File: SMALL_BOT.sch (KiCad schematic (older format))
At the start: 22 parts, among them J1 MOTOR_B, J10 HEADER_2, J11 Conn_01x04, J2 MOTOR_A, J3 HEADER_2, J4 HEADER_2, J5 Conn_01x04, J6 Conn_01x04, J7 Conn_01x04, J8 Conn_01x04, J9 HEADER_2, Q1 2N7002, U1 Teensy4.0, U2 DRV8833_POLOLU, U3 LM1117-SOT

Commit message: se modifico pcb
se movieron de lugar los conectores para los sensores ultrasonidos y se agrego pantalla oled
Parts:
- removed J3, J4: HEADER_2, EESTN5:Pin_strip_2, symbol EESTN5:HEADER_2
- removed U2: DRV8833_POLOLU, EESTN5:DRV8833_Pololu, symbol EESTN5:DRV8833_POLOLU
- added Brd1: SSD1306, SSD1306:128x64OLED, symbol SSD1306-128x64_OLED:SSD1306
- added C4, C6: 100nf, EESTN5:C_1206, symbol EESTN5:C
- added C5, C7: 100uf, EESTN5:CAP_TAN_A, symbol EESTN5:CAPAPOL
- added J12, J14: LEDS, EESTN5:Pin_Strip_3, symbol EESTN5:Conn_01X03
- added J13: I2C, EESTN5:pin_strip_4, symbol EESTN5:Conn_01x04
- added J15, J16, J3, J4: HEADER_1, EESTN5:Cable_Doble_1,5mm, symbol EESTN5:HEADER_1
- added R2, R3: 0,25, EESTN5:R_1206, symbol EESTN5:R
- added R? (x2): 10k, symbol EESTN5:R
- added U2, U4: DRV8872, EESTN5:SSOP-8, symbol EESTN5:DRV8872
- C1: value CAPAPOL -> 1000uf
- C2: value C -> 100nf
- C3: value CAPAPOL -> 10uf
- J5, J6, J7, J8: value Conn_01x04 -> ULTRASONICO; footprint EESTN5:HEADER-4H -> EESTN5:pin_strip_4
- R1: value R -> 10k
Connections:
- net labels added: NEOPIXEL, NEOPIXEL1, SCL, SDA
- wire segments 106 -> 161
- no-connect marks 0 -> 2
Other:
- moved on the sheet: BZ1, D1, Q1, R1

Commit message: Varios
Falta verificar al 100% la compatibilidad con los 3.3v para la Teensy.
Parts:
- removed U1: Teensy4.0, EESTN5:Teensy40, symbol EESTN5:Teensy4.0
- added U1: Teensy4.0_B, EESTN5:Teensy40_B, symbol EESTN5:Teensy4.0_B
- Brd1: symbol SSD1306-128x64_OLED:SSD1306 -> SMALL_BOT-rescue:SSD1306-SSD1306-128x64_OLED
- C6: value 100nf -> 100nF
- C7: value 100uf -> 100uF
- J1, J2: footprint EESTN5:Pololu_Micro_Gear_Motor_W_Mount -> EESTN5:Pololu_Micro_Con_Soporte_Simple
- J10: value HEADER_2 -> JMP
- J11: value Conn_01x04 -> UART
- J5, J6, J7, J8: value ULTRASONICO -> HC-SR04
- J9: value HEADER_2 -> Bateria
- R4, R5: renamed from R?; footprint (none) -> EESTN5:R_1206
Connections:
- wire segments 161 -> 157
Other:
- moved on the sheet: H1, J1, J2
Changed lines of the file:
@@
 $EndDescr
 $Comp
-L EESTN5:Teensy4.0 U1
-U 1 1 5FC8AD44
-P 2000 2300
-F 0 "U1" H 2000 3915 50  0000 C CNN
-F 1 "Teensy4.0" H 2000 3824 50  0000 C CNN
-F 2 "EESTN5:Teensy40" H 1600 2500 50  0001 C CNN
-F 3 "" H 1600 2500 50  0001 C CNN
-	1    2000 2300
-	1    0    0    -1
-$EndComp
-$Comp
 L EESTN5:HEADER_2 J1
 U 1 1 5FC8B78D
-P 10600 650
-F 0 "J1" H 10728 703 60  0000 L CNN
-F 1 "MOTOR_B" H 10728 597 60  0000 L CNN
-F 2 "EESTN5:Pololu_Micro_Gear_Motor_W_Mount" H 10600 900 60  0001 C CNN
-F 3 "" H 10600 900 60  0000 C CNN
-	1    10600 650
+P 10275 725
+F 0 "J1" H 10403 778 60  0000 L CNN
+F 1 "MOTOR_B" H 10403 672 60  0000 L CNN
+F 2 "EESTN5:Pololu_Micro_Con_Soporte_Simple" H 10275 975 60  0001 C CNN
+F 3 "" H 10275 975 60  0000 C CNN
+	1    10275 725
 	1    0    0    -1
 $EndComp
@@
 L EESTN5:HEADER_2 J2
 U 1 1 5FC8BAE6
-P 10600 850
-F 0 "J2" H 10728 903 60  0000 L CNN
-F 1 "MOTOR_A" H 10728 797 60  0000 L CNN
-F 2 "EESTN5:Pololu_Micro_Gear_Motor_W_Mount" H 10600 1100 60  0001 C CNN
-F 3 "" H 10600 1100 60  0000 C CNN
-	1    10600 850
+P 10275 925
+F 0 "J2" H 10403 978 60  0000 L CNN
+F 1 "MOTOR_A" H 10403 872 60  0000 L CNN
+F 2 "EESTN5:Pololu_Micro_Con_Soporte_Simple" H 10275 1175 60  0001 C CNN
+F 3 "" H 10275 1175 60  0000 C CNN
+	1    10275 925
 	1    0    0    -1
 $EndComp
@@
 L EESTN5:Mounting_Hole H1
 U 1 1 5FC8C238
-P 11100 700
-F 0 "H1" H 11200 700 50  0000 L CNN
-F 1 "Mounting_Hole" H 11100 825 50  0001 C CNN
-F 2 "EESTN5:Bateria_Lipo_2S_800mah" H 11100 700 60  0001 C CNN
-F 3 "" H 11100 700 60  0001 C CNN
-	1    11100 700
+P 10975 825
+F 0 "H1" H 11075 825 50  0000 L CNN
+F 1 "Mounting_Hole" H 10975 950 50  0001 C CNN
+F 2 "EESTN5:Bateria_Lipo_2S_800mah" H 10975 825 60  0001 C CNN
+F 3 "" H 10975 825 60  0001 C CNN
+	1    10975 825
 	1    0    0    -1
 $EndComp
@@
 P 1450 5150
 F 0 "J5" H 1530 5142 50  0000 L CNN
-F 1 "ULTRASONICO" H 1530 5051 50  0000 L CNN
+F 1 "HC-SR04" H 1530 5051 50  0000 L CNN
 F 2 "EESTN5:pin_strip_4" H 1450 5150 50  0001 C CNN
 F 3 "~" H 1450 5150 50  0001 C CNN
@@
 P 2750 5150
 F 0 "J7" H 2830 5142 50  0000 L CNN
-F 1 "ULTRASONICO" H 2830 5051 50  0000 L CNN
+F 1 "HC-SR04" H 2830 5051 50  0000 L CNN
 F 2 "EESTN5:pin_strip_4" H 2750 5150 50  0001 C CNN
 F 3 "~" H 2750 5150 50  0001 C CNN
@@
 P 1450 6400
 F 0 "J6" H 1530 6392 50  0000 L CNN
-F 1 "ULTRASONICO" H 1530 6301 50  0000 L CNN
+F 1 "HC-SR04" H 1530 6301 50  0000 L CNN
 F 2 "EESTN5:pin_strip_4" H 1450 6400 50  0001 C CNN
 F 3 "~" H 1450 6400 50  0001 C CNN
@@
 P 2750 6400
 F 0 "J8" H 2830 6392 50  0000 L CNN
-F 1 "ULTRASONICO" H 2830 6301 50  0000 L CNN
+F 1 "HC-SR04" H 2830 6301 50  0000 L CNN
 F 2 "EESTN5:pin_strip_4" H 2750 6400 50  0001 C CNN
 F 3 "~" H 2750 6400 50  0001 C CNN
@@
 U 1 1 5FD09509
 P 7500 5600
-F 0 "J9" H 7492 5313 60  0000 C CNN
-F 1 "HEADER_2" H 7500 5250 60  0000 C CNN
+F 0 "J9" H 7675 5575 60  0000 C CNN
+F 1 "Bateria" H 7575 5800 60  0000 C CNN
 F 2 "Connector_JST:JST_EH_B2B-EH-A_1x02_P2.50mm_Vertical" H 7500 5850 60  0001 C CNN
 F 3 "" H 7500 5850 60  0000 C CNN
@@
 F 1 "LM1117-SOT" H 9200 5701 60  0000 C CNN
 F 2 "EESTN5:SOT223" H 9200 5450 60  0001 C CNN
-F 3 "http://www.mouser.com/ds/2/282/lm1117-n-7107.pdf" H 9200 5595 60  0000 C CNN
+F 3 "http://www.mouser.com/ds/2/282/lm1117-n-7107.pdf" H 9200 5595 60  0001 C CNN
 	1    9200 5450
 	1    0    0    -1
@@
 U 1 1 5FD52493
 P 8150 5550
-F 0 "J10" V 8089 5678 60  0000 L CNN
-F 1 "HEADER_2" V 8195 5678 60  0000 L CNN
+F 0 "J10" V 8300 5475 60  0000 L CNN
+F 1 "JMP" V 8425 5475 60  0000 L CNN
 F 2 "EESTN5:Pin_strip_2" H 8150 5800 60  0001 C CNN
 F 3 "" H 8150 5800 60  0000 C CNN
@@
 P 4700 3350
 F 0 "J11" H 4780 3342 50  0000 L CNN
-F 1 "Conn_01x04" H 4780 3251 50  0000 L CNN
+F 1 "UART" H 4780 3251 50  0000 L CNN
 F 2 "EESTN5:pin_strip_4" H 4700 3350 50  0001 C CNN
 F 3 "~" H 4700 3350 50  0001 C CNN
@@
 Wire Wire Line
 	900  1150 650  1150
-Wire Wire Line
-	900  2550 750  2550
-Wire Wire Line
-	750  2550 750  3750
 $Comp
 L power:GND #PWR0123
 U 1 1 5FD87C3A
-P 750 3900
-F 0 "#PWR0123" H 750 3650 50  0001 C CNN
-F 1 "GND" H 755 3727 50  0000 C CNN
-F 2 "" H 750 3900 50  0001 C CNN
-F 3 "" H 750 3900 50  0001 C CNN
-	1    750  3900
+P 800 3900
+F 0 "#PWR0123" H 800 3650 50  0001 C CNN
+F 1 "GND" H 805 3727 50  0000 C CNN
+F 2 "" H 800 3900 50  0001 C CNN
+F 3 "" H 800 3900 50  0001 C CNN
+	1    800  3900
 	1    0    0    -1
 $EndComp
 Wire Wire Line
 	900  950  800  950
-Wire Wire Line
-	800  950  800  3750
-Wire Wire Line
-	800  3750 750  3750
-Connection ~ 750  3750
-Wire Wire Line
-	750  3750 750  3900
 $Comp
 L EESTN5:Conn_01X03 J12
@@
 NEOPIXEL
 $Comp
-L SSD1306-128x64_OLED:SSD1306 Brd1
+L SMALL_BOT-rescue:SSD1306-SSD1306-128x64_OLED Brd1
 U 1 1 5FE619BA
 P 10300 3600
-F 0 "Brd1" H 10022 3612 50  0000 R CNN
-F 1 "SSD1306" H 10022 3703 50  0000 R CNN
+F 0 "Brd1" H 10475 3200 50  0000 R CNN
+F 1 "SSD1306" H 10475 3300 50  0000 R CNN
 F 2 "SSD1306:128x64OLED" H 10300 3850 50  0001 C CNN
 F 3 "" H 10300 3850 50  0001 C CNN
@@
 P 5750 4550
 F 0 "J3" H 5878 4603 60  0000 L CNN
-F 1 "HEADER_1" H 5878 4497 60  0000 L CNN
+F 1 "HEADER_1" H 5878 4497 60  0001 L CNN
 F 2 "EESTN5:Cable_Doble_1,5mm" H 5750 4800 60  0001 C CNN
 F 3 "" H 5750 4800 60  0000 C CNN
@@
 P 5750 4750
 F 0 "J4" H 5878 4803 60  0000 L CNN
-F 1 "HEADER_1" H 6000 4850 60  0000 L CNN
+F 1 "HEADER_1" H 6000 4850 60  0001 L CNN
 F 2 "EESTN5:Cable_Doble_1,5mm" H 5750 5000 60  0001 C CNN
 F 3 "" H 5750 5000 60  0000 C CNN
@@
 P 5800 6350
 F 0 "J15" H 5928 6403 60  0000 L CNN
-F 1 "HEADER_1" H 5928 6297 60  0000 L CNN
+F 1 "HEADER_1" H 5928 6297 60  0001 L CNN
 F 2 "EESTN5:Cable_Doble_1,5mm" H 5800 6600 60  0001 C CNN
 F 3 "" H 5800 6600 60  0000 C CNN
@@
 P 5800 6550
 F 0 "J16" H 5928 6603 60  0000 L CNN
-F 1 "HEADER_1" H 6050 6650 60  0000 L CNN
+F 1 "HEADER_1" H 6050 6650 60  0001 L CNN
 F 2 "EESTN5:Cable_Doble_1,5mm" H 5800 6800 60  0001 C CNN
 F 3 "" H 5800 6800 60  0000 C CNN
@@
 U 1 1 5FF25413
 P 5600 6900
-F 0 "C6" H 5715 6938 40  0000 L CNN
-F 1 "100nf" H 5715 6862 40  0000 L CNN
+F 0 "C6" H 5325 6925 40  0000 L CNN
+F 1 "100nF" H 5325 6850 40  0000 L CNN
 F 2 "EESTN5:C_1206" H 5638 6750 30  0001 C CNN
 F 3 "" H 5600 6900 60  0000 C CNN
@@
 P 5900 6900
 F 0 "C7" H 6009 6938 40  0000 L CNN
-F 1 "100uf" H 6009 6862 40  0000 L CNN
+F 1 "100uF" H 6009 6862 40  0000 L CNN
 F 2 "EESTN5:CAP_TAN_A" H 6000 6750 30  0001 C CNN
 F 3 "" H 5900 6900 300 0000 C CNN
@@
 	9300 1450 9050 1450
 $Comp
-L EESTN5:R R?
+L EESTN5:R R4
 U 1 1 5FFAA029
 P 9300 3450
-F 0 "R?" H 9150 3500 50  0000 L CNN
+F 0 "R4" H 9150 3500 50  0000 L CNN
 F 1 "10k" H 9150 3400 50  0000 L CNN
-F 2 "" H 9300 3450 60  0000 C CNN
+F 2 "EESTN5:R_1206" H 9300 3450 60  0001 C CNN
 F 3 "" H 9300 3450 60  0000 C CNN
 	1    9300 3450
@@
 Connection ~ 9400 3700
 $Comp
-L EESTN5:R R?
+L EESTN5:R R5
 U 1 1 5FFAA29B
 P 9400 3450
-F 0 "R?" H 9448 3496 50  0000 L CNN
+F 0 "R5" H 9448 3496 50  0000 L CNN
 F 1 "10k" H 9448 3405 50  0000 L CNN
-F 2 "" H 9400 3450 60  0000 C CNN
+F 2 "EESTN5:R_1206" H 9400 3450 60  0001 C CNN
 F 3 "" H 9400 3450 60  0000 C CNN
 	1    9400 3450
@@
 	9400 3300 9400 3350
 Connection ~ 9300 3300
+$Comp
+L EESTN5:Teensy4.0_B U1
+U 1 1 5FD77C20
+P 2000 2300
+F 0 "U1" H 2000 3915 50  0000 C CNN
+F 1 "Teensy4.0_B" H 2000 3824 50  0000 C CNN
+F 2 "EESTN5:Teensy40_B" H 1600 2500 50  0001 C CNN
+F 3 "" H 1600 2500 50  0001 C CNN
+	1    2000 2300
+	1    0    0    -1
+$EndComp
+Wire Wire Line
+	800  950  800  3900
 $EndSCHEMATC

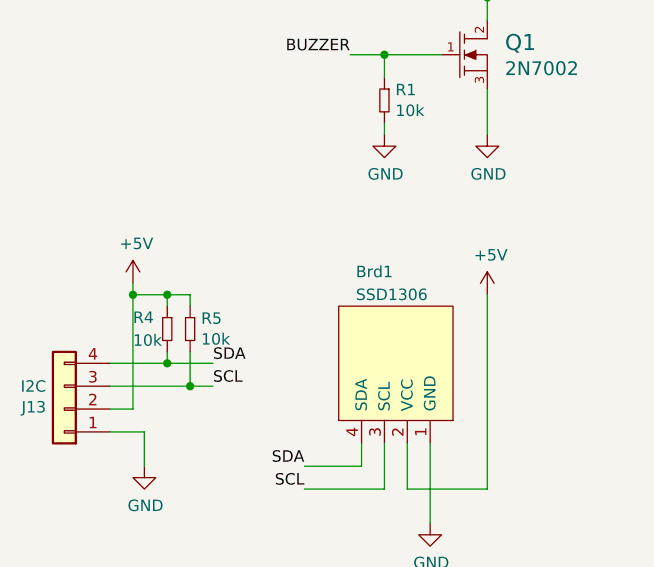
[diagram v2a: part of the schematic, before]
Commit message: Pantalla Oled
Actualice la pantalla oled
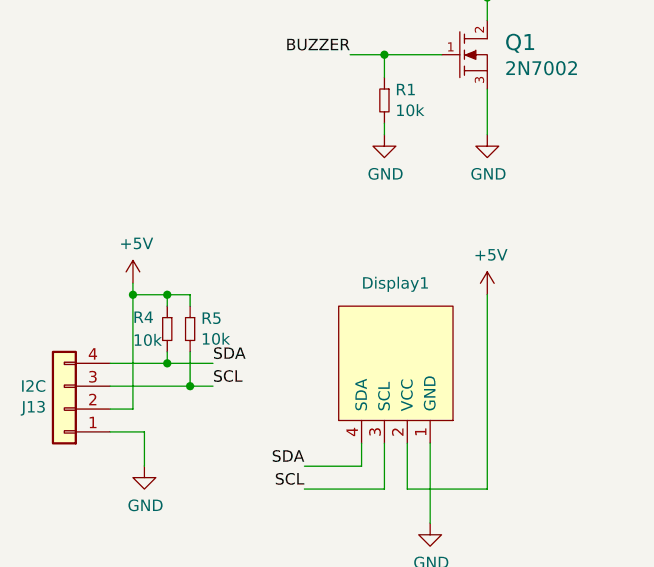
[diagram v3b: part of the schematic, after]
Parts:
- removed Brd1: SSD1306, SSD1306:128x64OLED, symbol SMALL_BOT-rescue:SSD1306-SSD1306-128x64_OLED
- added Display1: SSD1306-SSD1306-128x64_OLED, EESTN5:128x64OLED, symbol EESTN5:SSD1306-SSD1306-128x64_OLED
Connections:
- net +5V: now also Display1.2 (VCC)
- net GND: now also Display1.1 (GND)
- net SCL: now also Display1.3 (SCL)
- net SDA: now also Display1.4 (SDA)
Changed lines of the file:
@@
 Text Label 700  1450 2    50   ~ 0
 NEOPIXEL
-$Comp
-L SMALL_BOT-rescue:SSD1306-SSD1306-128x64_OLED Brd1
-U 1 1 5FE619BA
-P 10300 3600
-F 0 "Brd1" H 10475 3200 50  0000 R CNN
-F 1 "SSD1306" H 10475 3300 50  0000 R CNN
-F 2 "SSD1306:128x64OLED" H 10300 3850 50  0001 C CNN
-F 3 "" H 10300 3850 50  0001 C CNN
-	1    10300 3600
-	-1   0    0    1
-$EndComp
 Wire Wire Line
 	10150 3950 10150 4050
@@
 Wire Wire Line
 	800  950  800  3900
+$Comp
+L EESTN5:SSD1306-SSD1306-128x64_OLED Display1
+U 1 1 5FD81AE7
+P 10300 3600
+F 0 "Display1" H 10450 3250 50  0000 R CNN
+F 1 "SSD1306-SSD1306-128x64_OLED" H 10300 3550 50  0001 C CNN
+F 2 "EESTN5:128x64OLED" H 10300 3850 50  0001 C CNN
+F 3 "" H 10300 3850 50  0001 C CNN
+	1    10300 3600
+	-1   0    0    1
+$EndComp
 $EndSCHEMATC

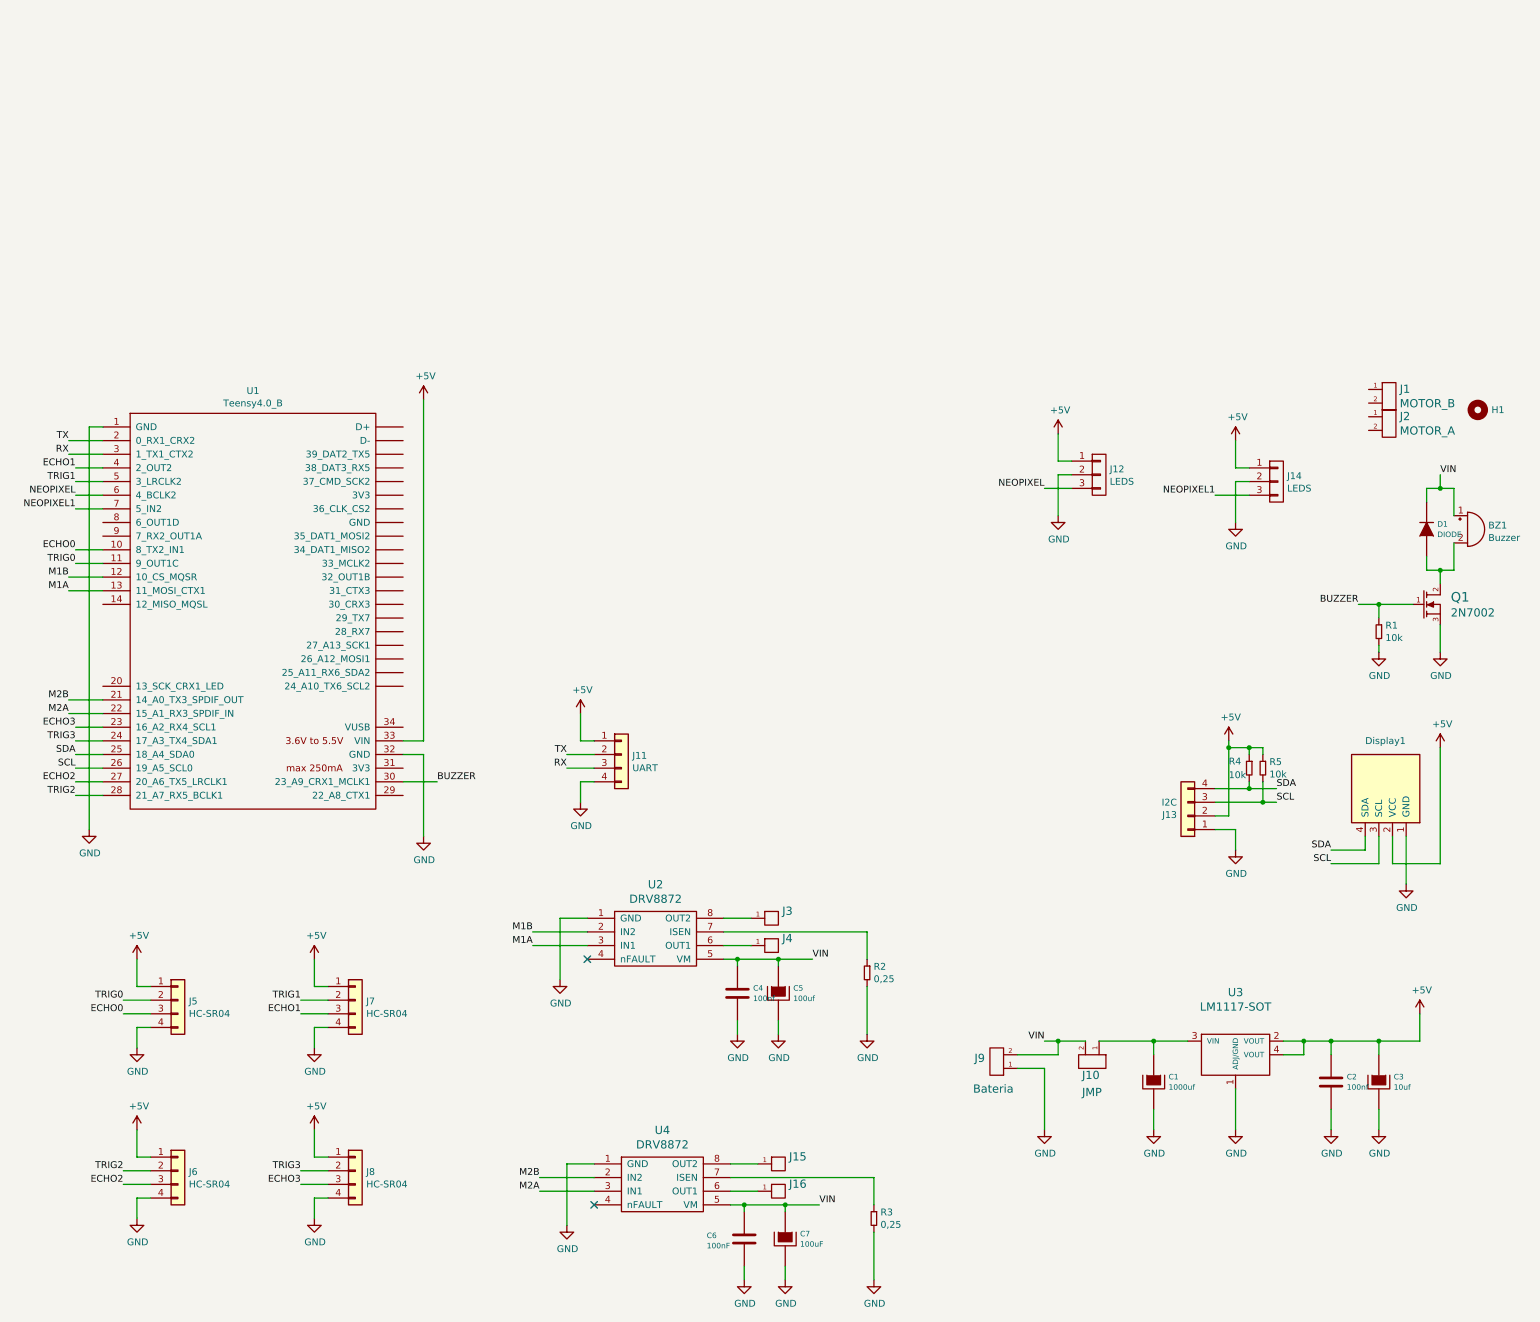
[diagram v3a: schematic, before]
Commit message: modificaciones
se agrego una brebe pinout, se agrego una carpeta "doc" y lista de materiales, hay que agregarle los precios.tambien se modifico el pcb
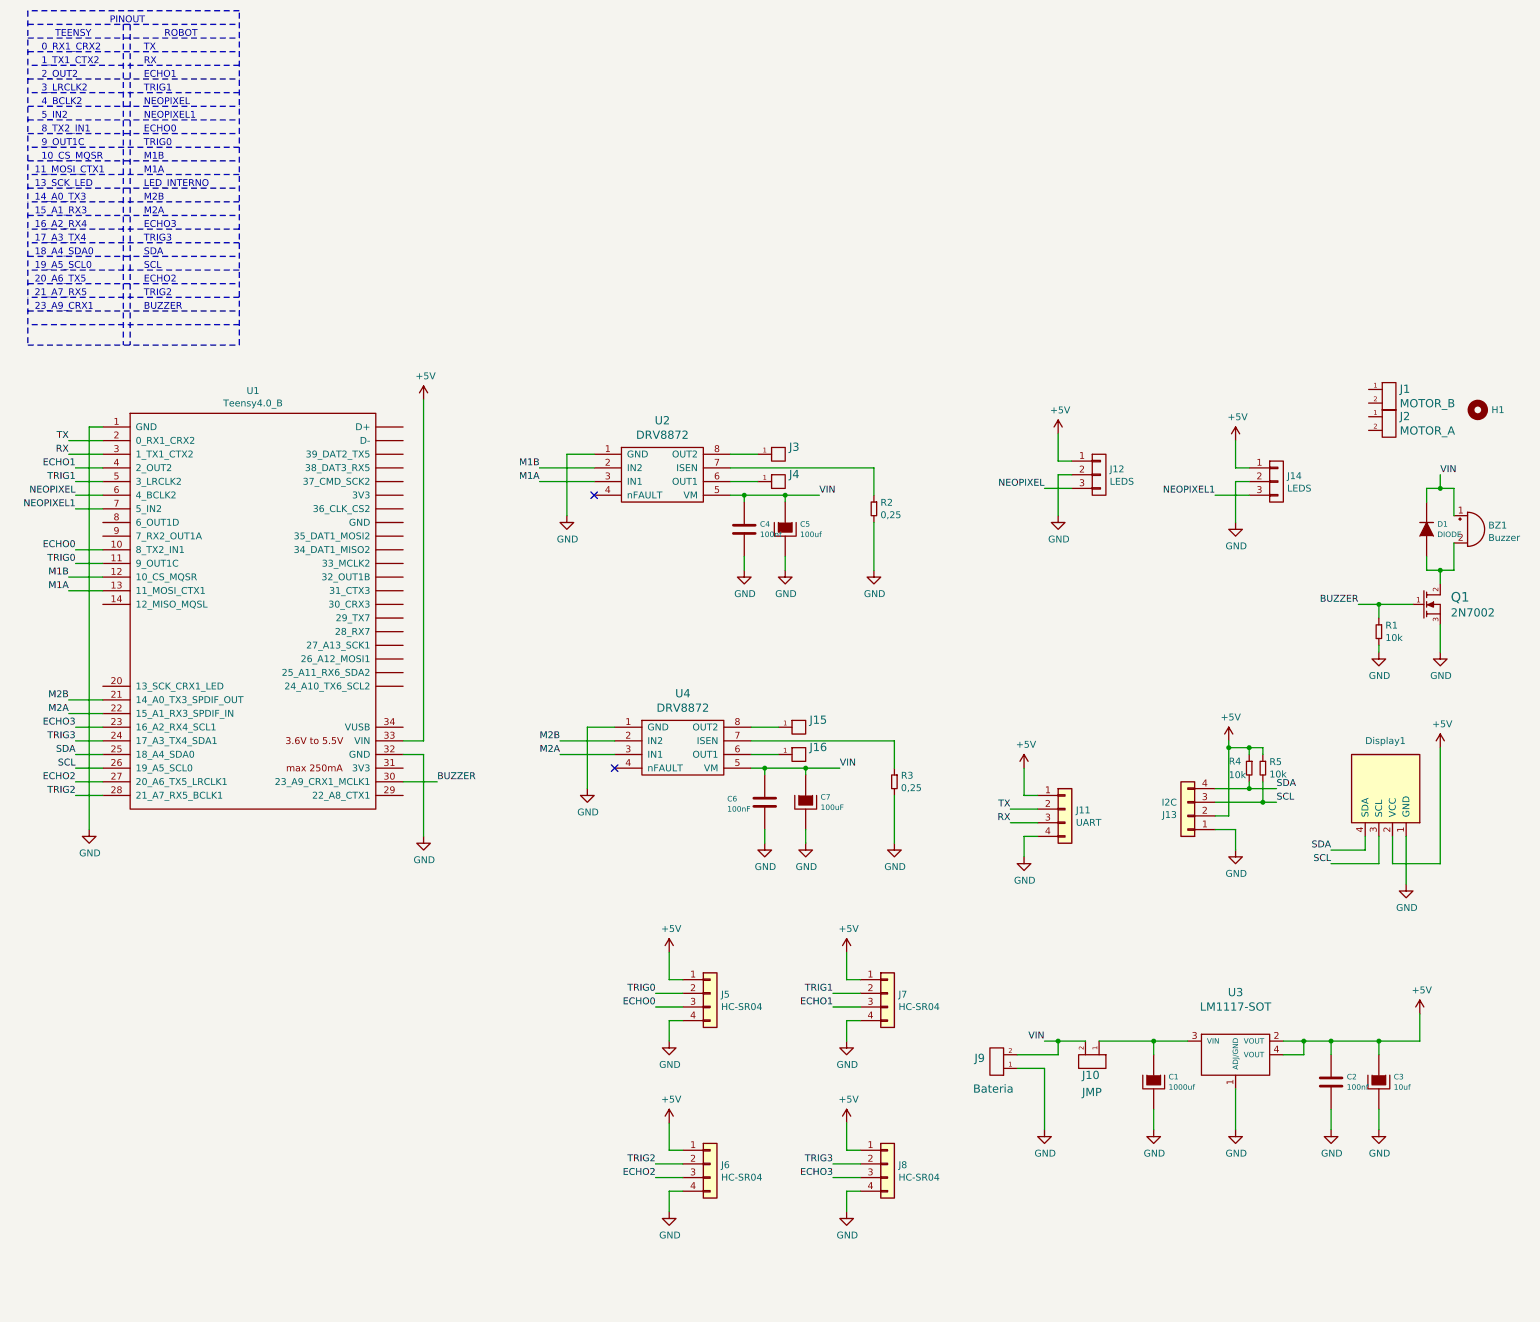
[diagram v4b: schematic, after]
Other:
- note added: "0_RX1_CRX2"
- note added: "10_CS_MQSR\n"
- note added: "11_MOSI_CTX1\n"
- note added: "13_SCK_LED"
- note added: "14_A0_TX3"
- note added: "15_A1_RX3"
- note added: "16_A2_RX4"
- note added: "17_A3_TX4"
- note added: "18_A4_SDA0"
- note added: "19_A5_SCL0"
- note added: "1_TX1_CTX2"
- note added: "20_A6_TX5"
- note added: "21_A7_RX5"
- note added: "23_A9_CRX1\n"
- note added: "2_OUT2"
- note added: "3_LRCLK2"
- note added: "4_BCLK2"
- note added: "5_IN2"
- note added: "8_TX2_IN1"
- note added: "9_OUT1C"
- note added: "BUZZER"
- note added: "ECHO0"
- note added: "ECHO1"
- note added: "ECHO2"
- note added: "ECHO3"
- note added: "LED_INTERNO"
- note added: "M1A"
- note added: "M1B"
- note added: "M2A"
- note added: "M2B"
- note added: "NEOPIXEL"
- note added: "NEOPIXEL1"
- note added: "PINOUT"
- note added: "ROBOT\n"
- note added: "RX"
- note added: "SCL"
- note added: "SDA"
- note added: "TEENSY\n"
- note added: "TRIG0"
- note added: "TRIG1"
- note added: "TRIG2"
- note added: "TRIG3"
- note added: "TX"
- moved on the sheet: C4, C5, C6, C7, J11, J15, J16, J3, J4, J5, J6, J7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
